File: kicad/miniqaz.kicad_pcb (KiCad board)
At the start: 2 copper layers, 124 x 57.3 mm, 43 parts, among them U1 

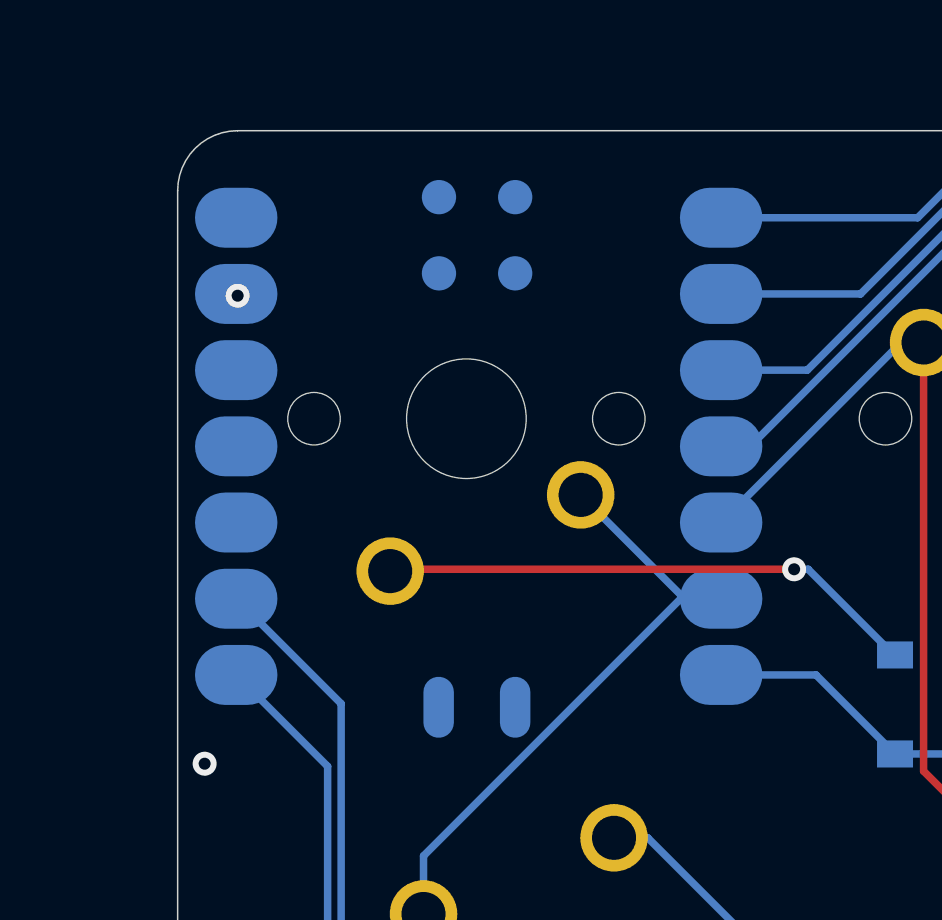
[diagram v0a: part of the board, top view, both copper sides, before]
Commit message: design updates
- Added relative Path for MX-Switch lib
- Modified Seeeduino Xiao footprint to move origin to the center
- Centered Seeeduino Xia Footprint under the top-left key
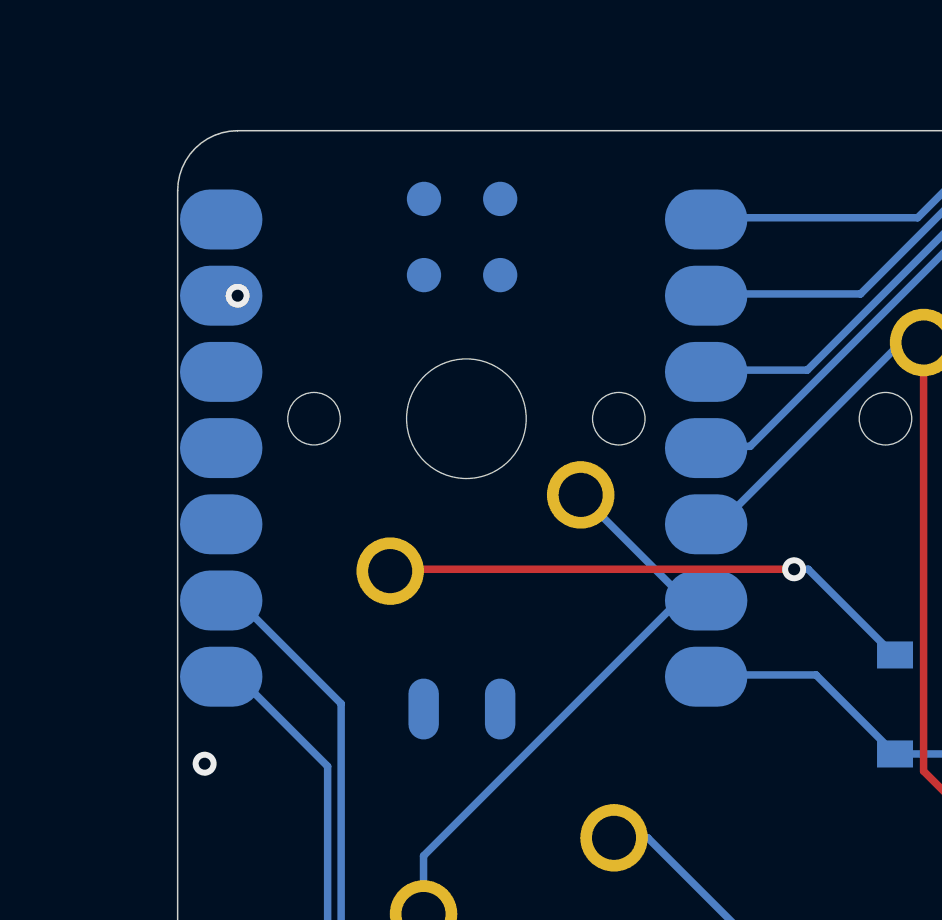
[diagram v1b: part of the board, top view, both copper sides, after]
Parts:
- moved U1 14.0 mm to (142.5, 79.0)
